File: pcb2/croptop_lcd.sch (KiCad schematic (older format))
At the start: 66 parts, among them J4 TSM-102-01-L-DV, J5 686104183422, J6 62684-402100ALF, U10 TPD4E1U06DBV, U11 TPD4E1U06DBV, U12 TPD4E1U06DBV, U13 TPD4E1U06DBV, U14 TPD4E1U06DBV, U15 TPD4E1U06DBV, U16 TPD4E1U06DBV, U17 TPD4E1U06DBV, U8 TPD4E1U06DBV, U9 FT812Q, Y2 ABLS-12.000MHZ-B2-T

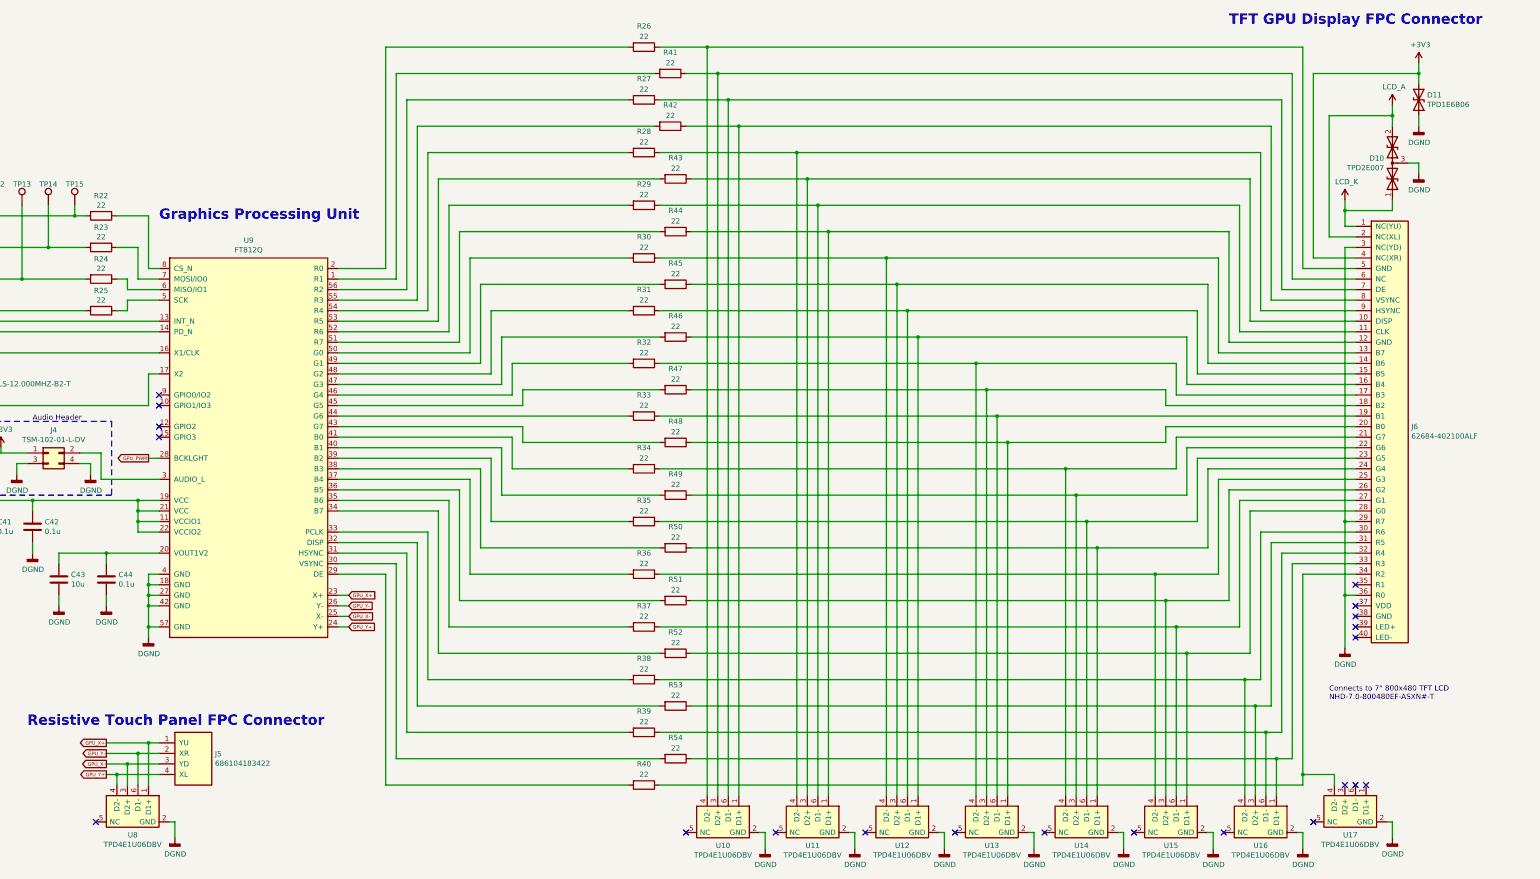
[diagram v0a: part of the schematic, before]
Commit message: Fixed Screen alignment
- Fixed pin alignment of LCD screen
- Pins now properly align with the ribbon cables of the LCD screen
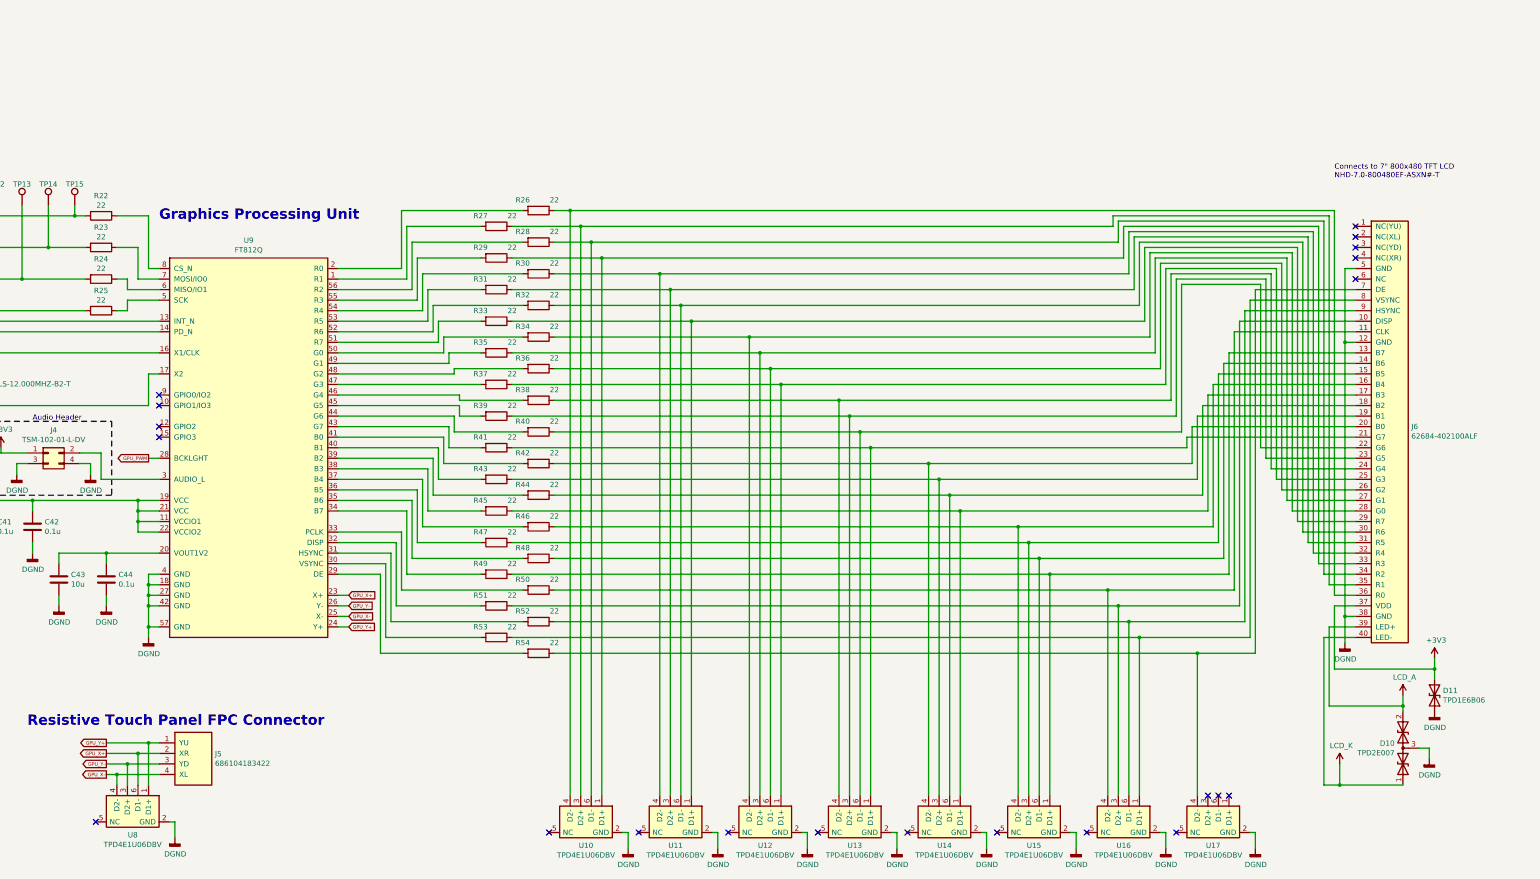
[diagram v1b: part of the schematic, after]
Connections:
- net +3V3: now also J6.37 (VDD); no longer J6.4 (NC(XR))
- net DGND: now also J6.12 (GND), J6.38 (GND), J6.5 (GND); no longer J6.29 (R7), J6.3 (NC(YD)), J6.36 (R0)
- net GPU_X+: now also J5.2 (XR), U8.6 (D1-); no longer J5.1 (YU), U8.1 (D1+)
- net GPU_X-: now also J5.4 (XL), U8.4 (D2-); no longer J5.3 (YD), U8.3 (D2+)
- net GPU_Y+: now also J5.1 (YU), U8.1 (D1+); no longer J5.4 (XL), U8.4 (D2-)
- net GPU_Y-: now also J5.3 (YD), U8.3 (D2+); no longer J5.2 (XR), U8.6 (D1-)
- net LCD_A: now also J6.39 (LED+); no longer J6.2 (NC(XL))
- net LCD_K: now also J6.40 (LED-); no longer J6.1 (NC(YU))
- net at U9.1 (R1): now also R27.2; no longer R41.2
- net at U9.29 (DE): now also R54.2; no longer R40.2
- net at U9.30 (VSYNC): now also R53.2; no longer R54.2
- net at U9.31 (HSYNC): now also R52.2; no longer R39.2
- net at U9.32 (DISP): now also R51.2; no longer R53.2
- net at U9.33 (PCLK): now also R50.2; no longer R38.2
- net at U9.34 (B7): now also R49.2; no longer R52.2
- net at U9.35 (B6): now also R48.2; no longer R37.2
- net at U9.36 (B5): now also R47.2; no longer R51.2
- net at U9.37 (B4): now also R46.2; no longer R36.2
- net at U9.38 (B3): now also R45.2; no longer R50.2
- net at U9.39 (B2): now also R44.2; no longer R35.2
- net at U9.40 (B1): now also R43.2; no longer R49.2
- net at U9.41 (B0): now also R42.2; no longer R34.2
- net at U9.43 (G7): now also R41.2; no longer R48.2
- net at U9.44 (G6): now also R40.2; no longer R33.2
- net at U9.45 (G5): now also R39.2; no longer R47.2
- net at U9.46 (G4): now also R38.2; no longer R32.2
- net at U9.47 (G3): now also R37.2; no longer R46.2
- net at U9.48 (G2): now also R36.2; no longer R31.2
- net at U9.49 (G1): now also R35.2; no longer R45.2
- net at U9.50 (G0): now also R34.2; no longer R30.2
- net at U9.51 (R7): now also R33.2; no longer R44.2
- net at U9.52 (R6): now also R32.2; no longer R29.2
- net at U9.53 (R5): now also R31.2; no longer R43.2
- net at U9.54 (R4): now also R30.2; no longer R28.2
- net at U9.55 (R3): now also R29.2; no longer R42.2
- net at U9.56 (R2): now also R28.2; no longer R27.2
- net at J6.16 (B4), R46.1: now also U15.4 (D2-); no longer U12.1 (D1+)
- net at J6.35 (R1): now also R27.1, U10.3 (D2+)
- net at R26.1, U10.4 (D2-): now also J6.36 (R0); no longer J6.5 (GND)
- new net: J6.10 (DISP), R51.1, U16.3 (D2+)
- new net: J6.11 (CLK), R50.1, U16.4 (D2-)
- new net: J6.13 (B7), R49.1, U15.1 (D1+)
- new net: J6.14 (B6), R48.1, U15.6 (D1-)
- new net: J6.15 (B5), R47.1, U15.3 (D2+)
- new net: J6.17 (B3), R45.1, U14.1 (D1+)
- new net: J6.18 (B2), R44.1, U14.6 (D1-)
- new net: J6.19 (B1), R43.1, U14.3 (D2+)
- new net: J6.20 (B0), R42.1, U14.4 (D2-)
- new net: J6.21 (G7), R41.1, U13.1 (D1+)
- new net: J6.22 (G6), R40.1, U13.6 (D1-)
- new net: J6.23 (G5), R39.1, U13.3 (D2+)
- new net: J6.24 (G4), R38.1, U13.4 (D2-)
- new net: J6.25 (G3), R37.1, U12.1 (D1+)
- new net: J6.26 (G2), R36.1, U12.6 (D1-)
- new net: J6.27 (G1), R35.1, U12.3 (D2+)
- new net: J6.28 (G0), R34.1, U12.4 (D2-)
- new net: J6.29 (R7), R33.1, U11.1 (D1+)
- new net: J6.30 (R6), R32.1, U11.6 (D1-)
- new net: J6.31 (R5), R31.1, U11.3 (D2+)
- new net: J6.32 (R4), R30.1, U11.4 (D2-)
- new net: J6.33 (R3), R29.1, U10.1 (D1+)
- new net: J6.34 (R2), R28.1, U10.6 (D1-)
- new net: J6.7 (DE), R54.1, U17.4 (D2-)
- new net: J6.8 (VSYNC), R53.1, U16.1 (D1+)
- new net: J6.9 (HSYNC), R52.1, U16.6 (D1-)
- now unconnected: J6.6 (NC)
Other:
- note removed: "TFT GPU Display FPC Connector"
- moved on the sheet: D10, D11, U10, U11, U12, U13, U14, U15, U16, U17
